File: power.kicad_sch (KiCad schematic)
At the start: 34 parts, among them J2 KYCO-P4S-S, J3 MicroFit_2x02, J3B1 DNI, J4 DC 24V/5A OUT, Q1 BC857, Q2 IRF9540SPBF, SW1 DNI, U1 MAX5035BUSA, U6 MC78M12BDTG

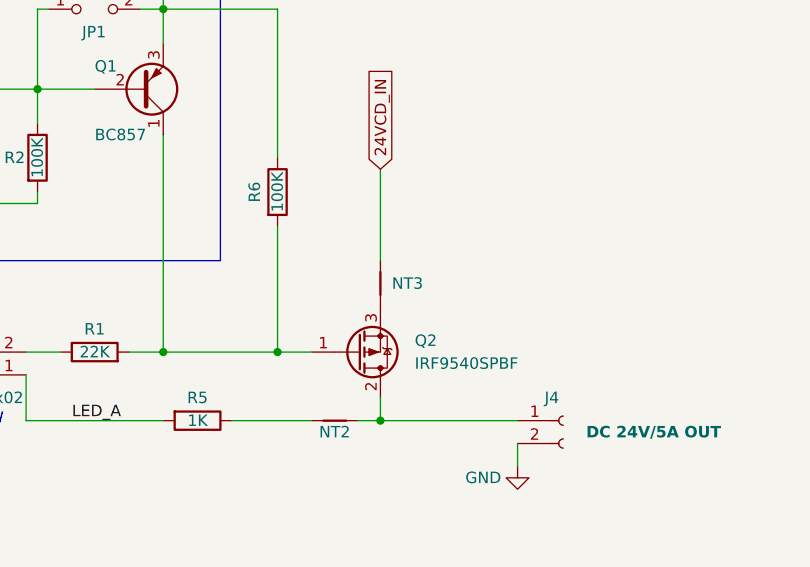
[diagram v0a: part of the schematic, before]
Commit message: Much to do about OCD power distribution. (Removed all loop 'antennas' and balanced transmission lines..)
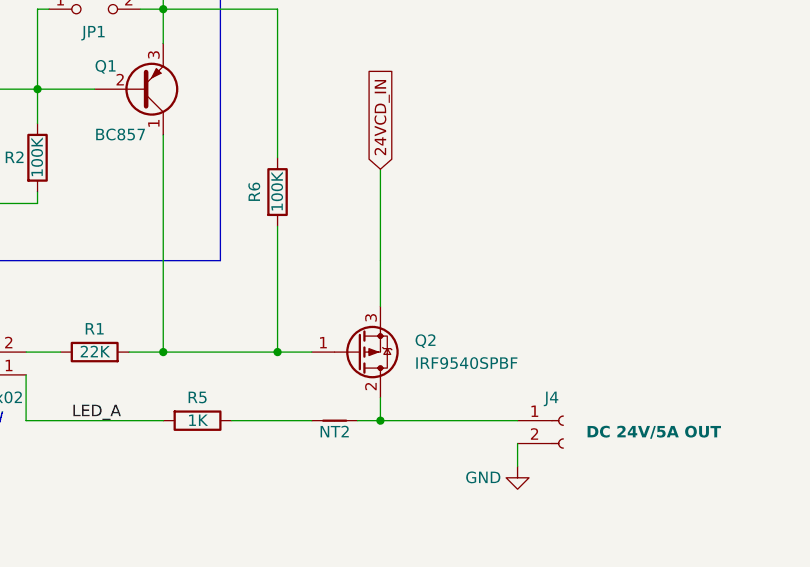
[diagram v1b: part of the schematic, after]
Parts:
- removed NT3: DNI, NetTie:NetTie-2_SMD_Pad2.0mm, symbol Device:NetTie_2
- NT1: footprint NetTie:NetTie-2_SMD_Pad2.0mm -> _footprints:NetTie-2_SMD_Pad0.5mm
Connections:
- net 24VCD_IN: now also Q2.3 (S)
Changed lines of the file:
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@@
+    (stroke (width 0) (type default) (color 0 0 0 0))
+  )
+  (wire (pts (xy 158.75 99.06) (xy 158.75 104.14))
     (stroke (width 0) (type default) (color 0 0 0 0))
   )
@@
     (pin "2")
   )
-  (symbol (lib_id "Device:NetTie_2") (at 158.75 101.6 90) (unit 1)
-    (in_bom yes) (on_board yes) (fields_autoplaced)
-    (property "Reference" "NT3" (id 0) (at 160.02 101.5999 90)
-      (effects (font (size 1.27 1.27)) (justify right))
-    )
-    (property "Value" "DNI" (id 1) (at 160.02 102.8699 90)
-      (effects (font (size 1.27 1.27)) (justify right) hide)
-    )
-    (property "Footprint" "NetTie:NetTie-2_SMD_Pad2.0mm" (id 2) (at 158.75 101.6 0)
-      (effects (font (size 1.27 1.27)) hide)
-    )
-    (property "Datasheet" "~" (id 3) (at 158.75 101.6 0)
-      (effects (font (size 1.27 1.27)) hide)
-    )
-    (pin "1")
-    (pin "2")
-  )
   (symbol (lib_id "Device:NetTie_2") (at 153.67 116.84 0) (unit 1)
     (in_bom yes) (on_board yes)
@@
       (effects (font (size 1.27 1.27)) hide)
     )
-    (property "Footprint" "NetTie:NetTie-2_SMD_Pad2.0mm" (id 2) (at 58.42 41.91 0)
-      (effects (font (size 1.27 1.27)) hide)
-    )
+    (property "Footprint" "_footprints:NetTie-2_SMD_Pad0.5mm" (id 2) (at 58.42 41.91 0)
+      (effects (font (size 1.27 1.27)) hide)
+    )

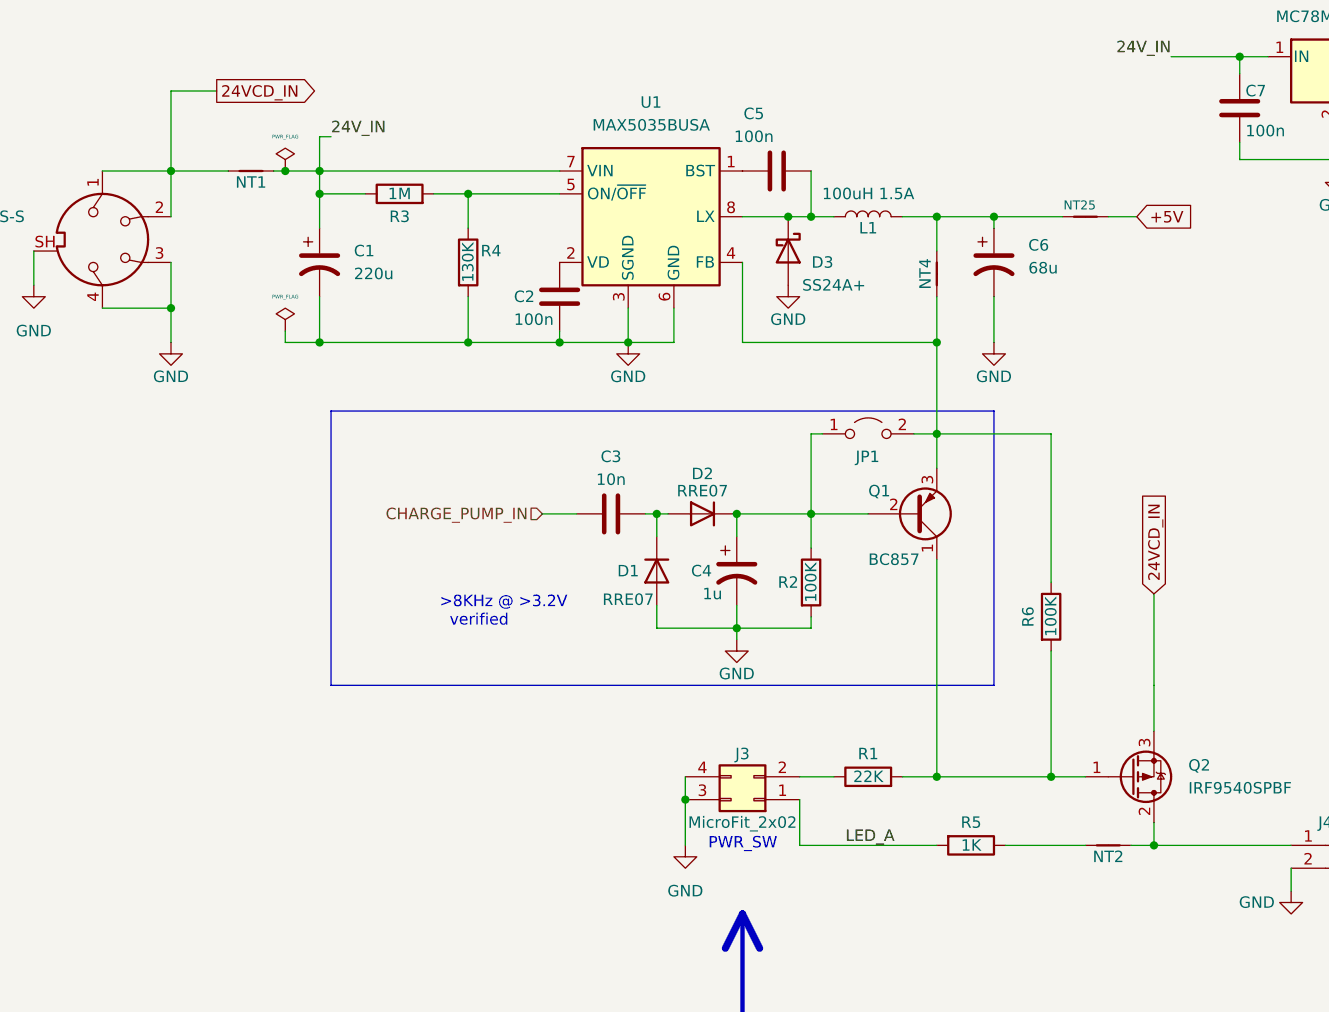
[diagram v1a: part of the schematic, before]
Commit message: Probe connectors wired wrong. Improved 5V buck reg layout.
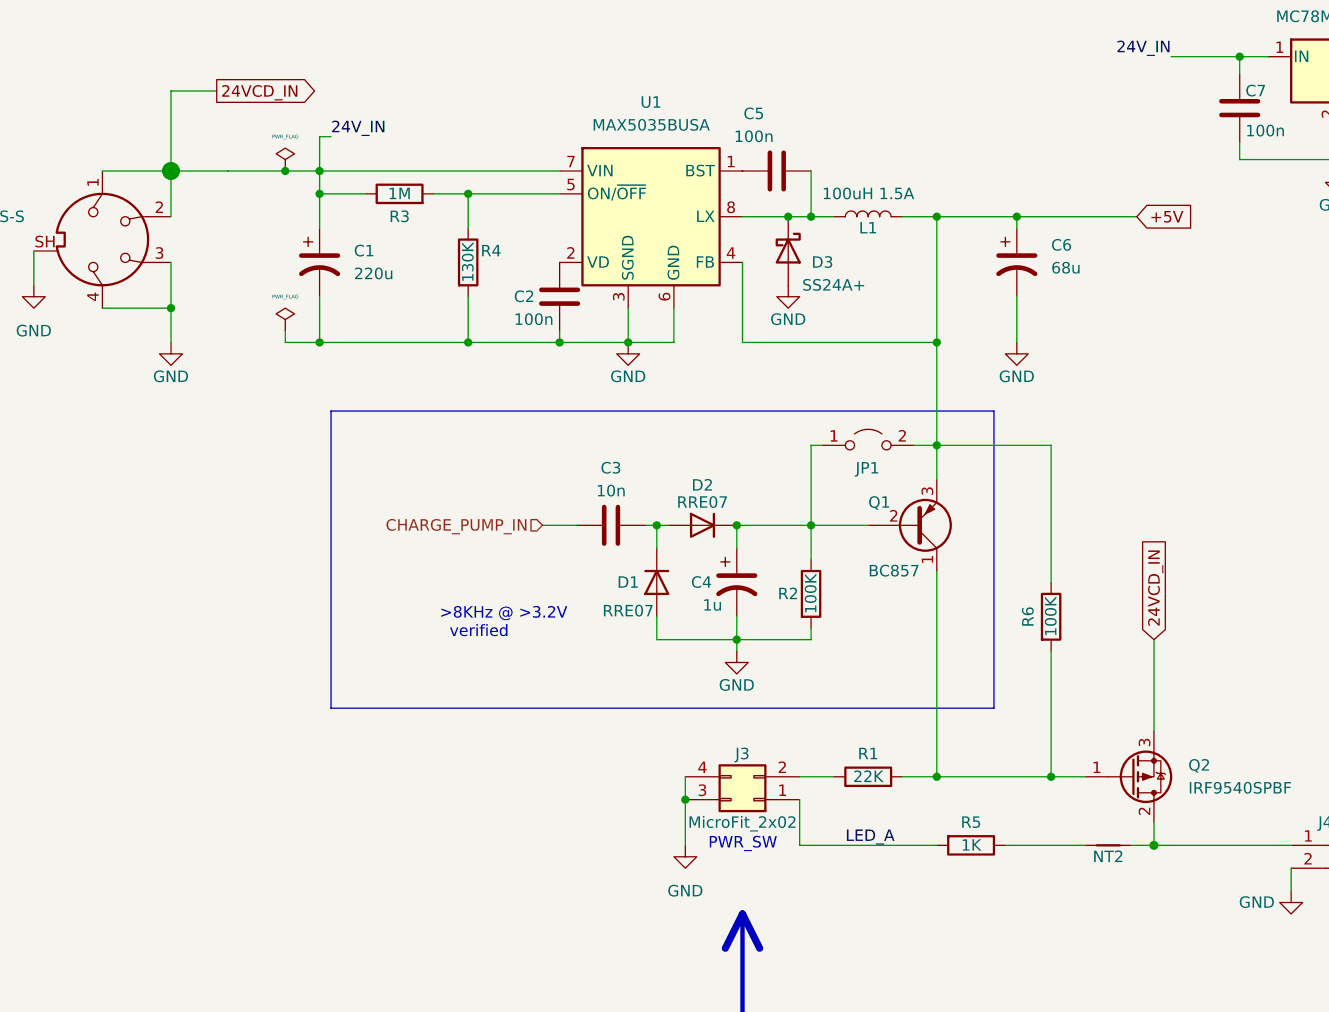
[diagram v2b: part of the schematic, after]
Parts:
- removed NT1, NT25, NT4: DNI, _footprints:NetTie-2_SMD_Pad0.5mm, symbol Device:NetTie_2
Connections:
- net 24V_IN is gone; now on net 24VCD_IN: C1.1, C7.1, R3.1, U1.7 (VIN), U6.1 (IN)
- net +5V: now also C6.1, JP1.2 (B), L1.2, Q1.3 (E), R6.1, U1.4 (FB)
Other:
- moved on the sheet: C3, C4, C6, D1, D2, JP1, Q1, R2

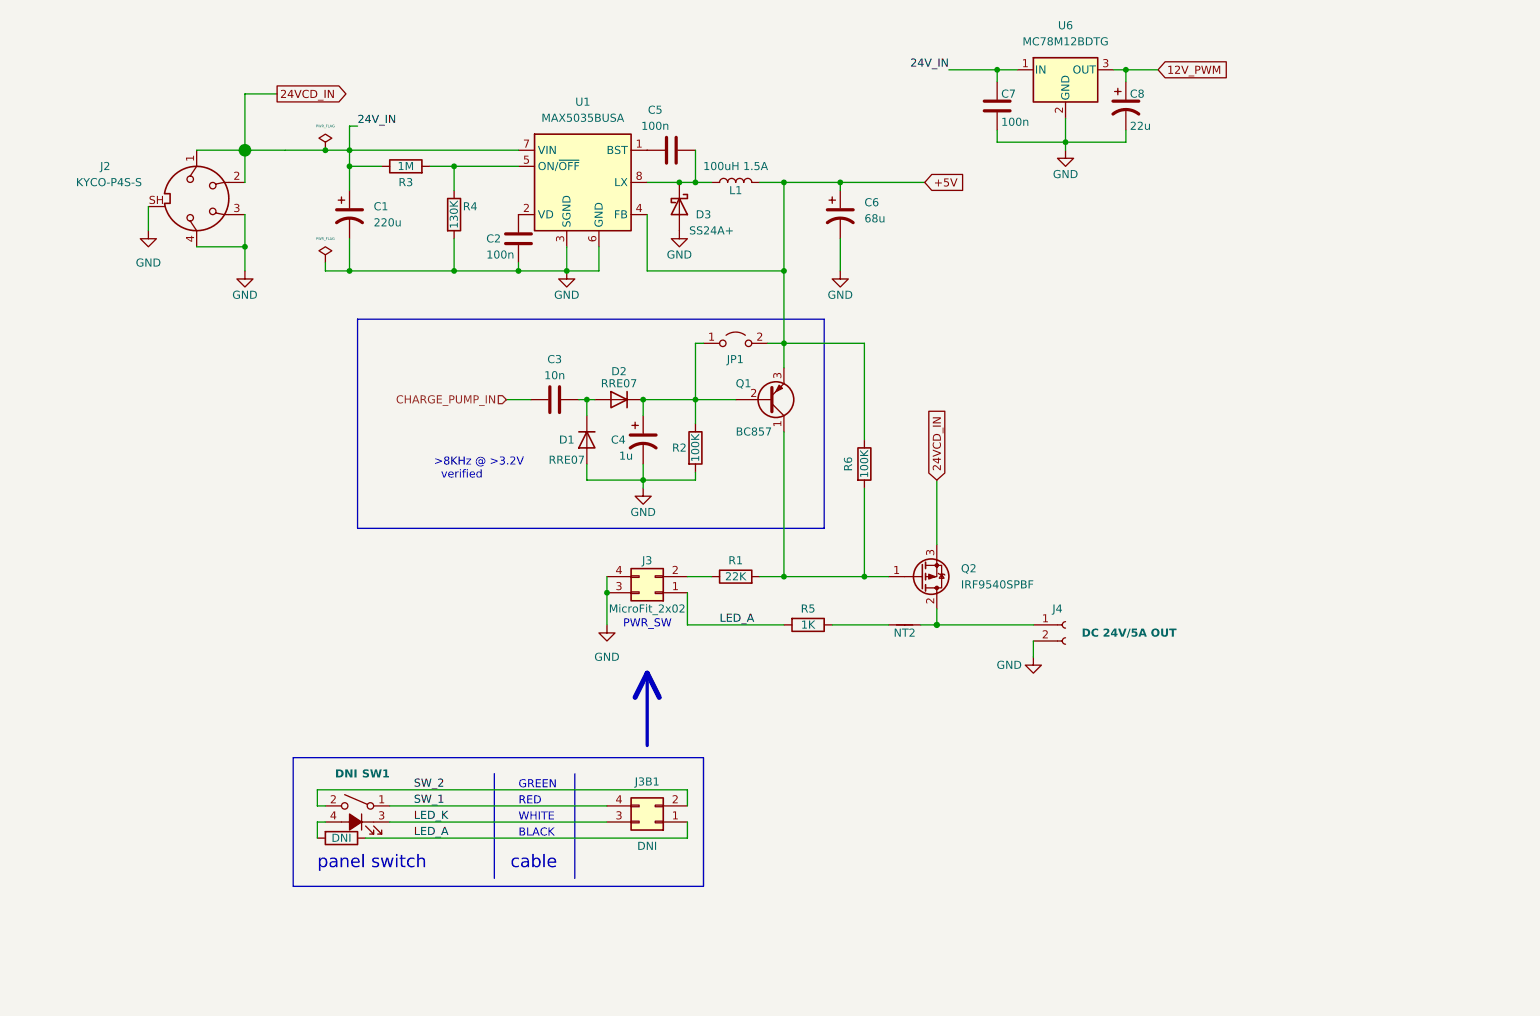
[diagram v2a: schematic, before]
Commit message: Added LEDs (more coming). Changes to charge pump and related power switching.
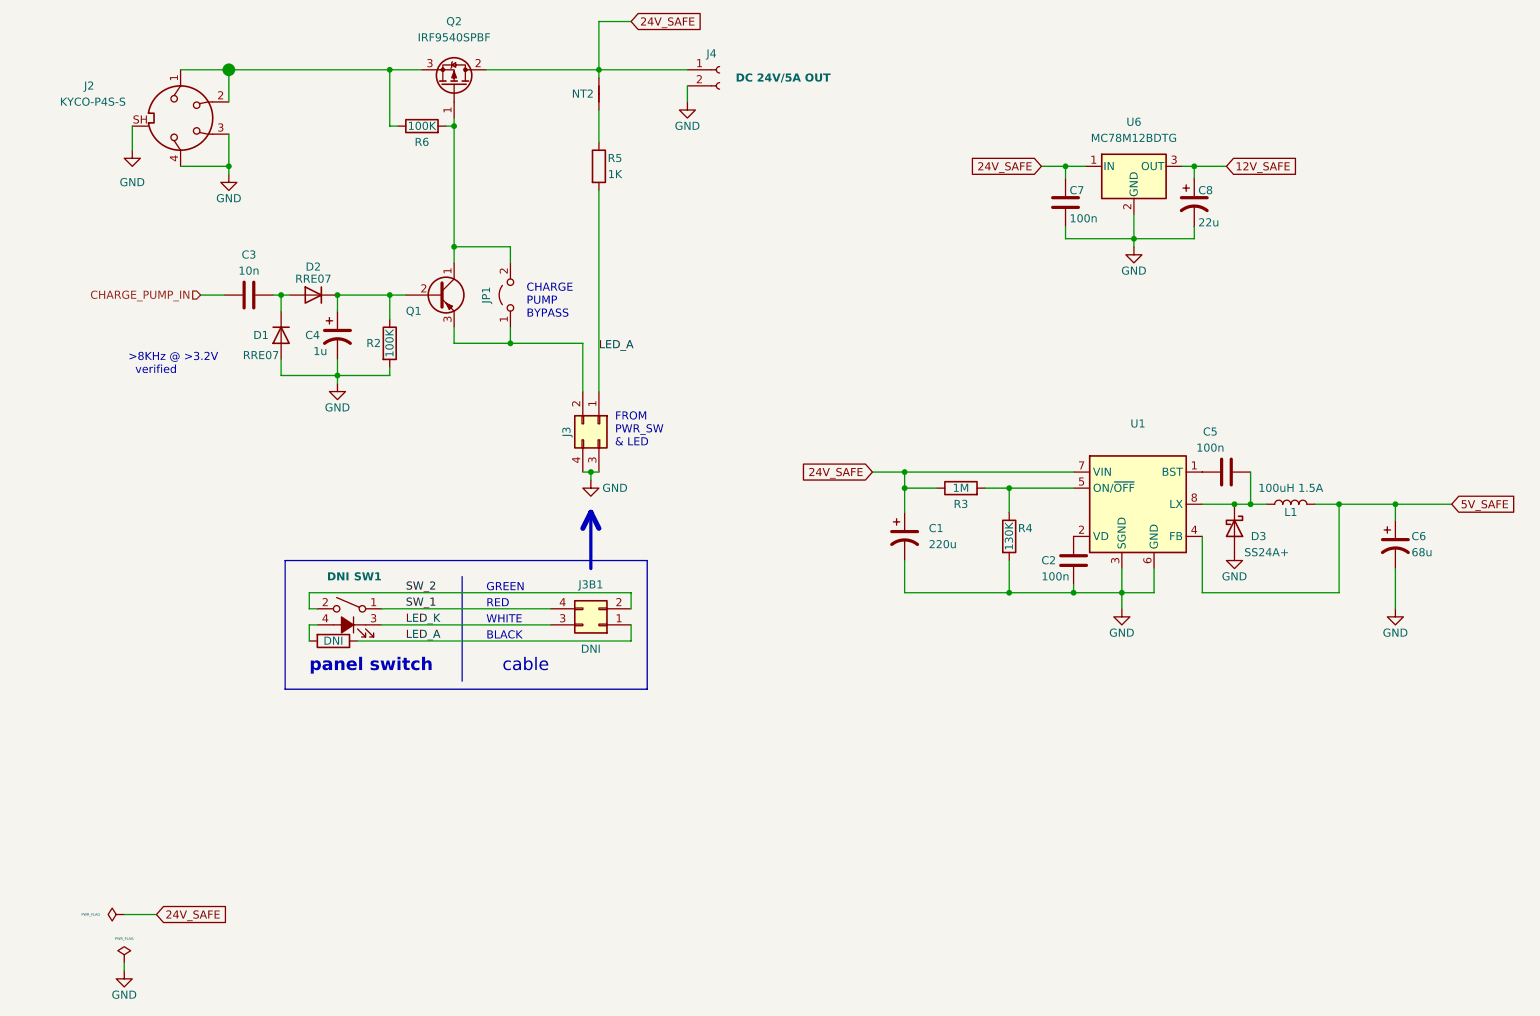
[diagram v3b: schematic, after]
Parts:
- removed R1: 22K, Resistor_SMD:R_0603_1608Metric, symbol Device:R
- J3: value MicroFit_2x02 -> (none)
- Q1: value BC857 -> (none); footprint Package_TO_SOT_SMD:SOT-23 -> Package_TO_SOT_THT:TO-92_Inline
- U1: value MAX5035BUSA -> (none)
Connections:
- net at Q1.1 (C), Q2.1 (G), R6.2: now also JP1.2 (B)
- net at C4.1, D2.1 (K), Q1.2 (B)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: no longer JP1.1 (A)
- net 24V_SAFE: now reaches J4.1 (Pin_1), NT2.2, Q2.2 (D)
- net 24V_SAFE: now also C1.1, C7.1, R3.1, U1.7 (VIN), U6.1 (IN)
- net at J3.2 (Pin_2): now also JP1.1 (A), Q1.3 (E)
- net +5V renamed 5V_SAFE
- net 5V_SAFE: no longer JP1.2 (B), Q1.3 (E), R6.1
- net 12V_PWM renamed 12V_SAFE
- removed net 24VCD_IN: C1.1, C7.1, J2.1, J2.2, Q2.3 (S), R3.1, U1.7 (VIN), U6.1 (IN)
- new net: J2.1, J2.2, Q2.3 (S), R6.1
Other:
- note added: "CHARGE PUMP BYPASS"
- note added: "FROM PWR_SW & LED"
- note removed: "PWR_SW"
- moved on the sheet: C1, C2, C3, C4, C5, C6, C7, C8, D1, D2, D3, J2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

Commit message: Forgot R1 and more NT fun.
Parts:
- added R1: (no value), Resistor_SMD:R_0603_1608Metric, symbol Device:R
- J3: value (none) -> MicroFit_2x02
- Q1: symbol Transistor_BJT:BC557 -> Transistor_BJT:BC547
- R2: value 100K -> (none)
- U1: value (none) -> MAX5035BUSA
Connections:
- net at C4.1, D2.1 (K): now also R1.1; no longer Q1.2 (B), R2.1
- net 5V_SAFE renamed +5V
- new net: Q1.2 (B), R1.2, R2.1
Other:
- moved on the sheet: C3, C4, D1, D2, R2
